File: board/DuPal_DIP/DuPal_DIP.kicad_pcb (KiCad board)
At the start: 2 copper layers, 113 x 78.7 mm, 56 parts, among them J1 AVR-ISP-6, J2 RS232, J3 Power IN, SW1 SW_Push, SW2 Power, U1 ATmega8A-PU, U10 24 Pin PAL, U2 74HC595, U3 74HC595, U5 20 Pin PAL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

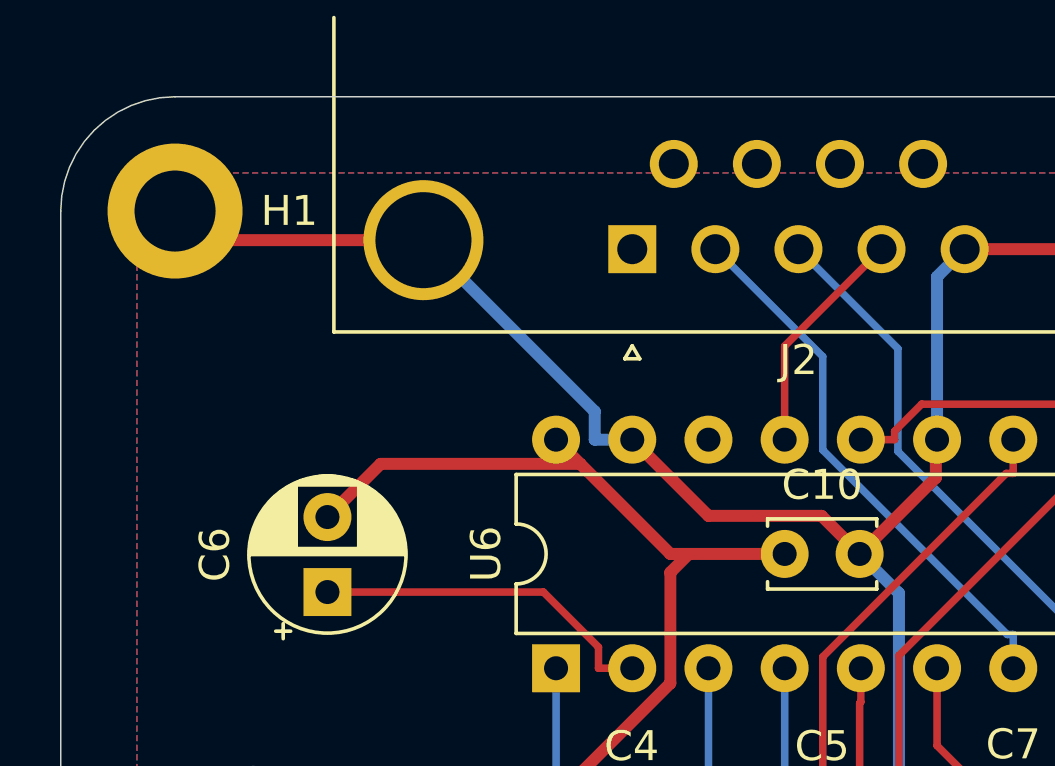
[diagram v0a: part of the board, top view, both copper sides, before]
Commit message: Updated silkscreen
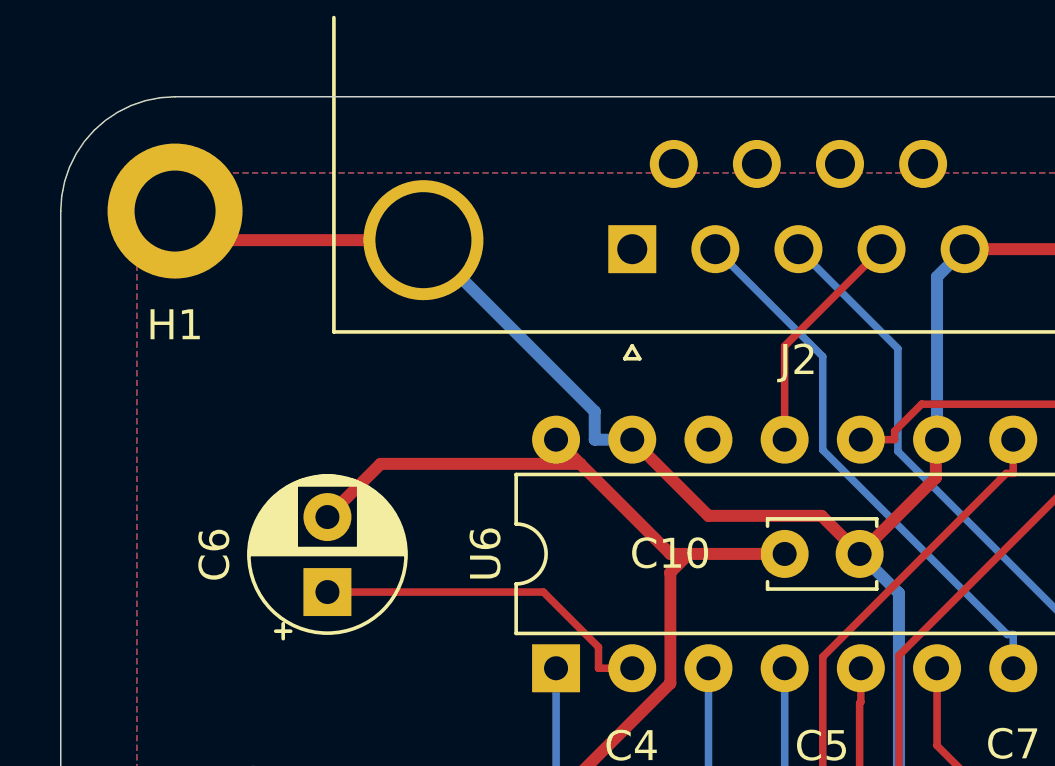
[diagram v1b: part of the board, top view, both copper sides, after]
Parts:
- added G***: LOGO, logo:logo, B.Cu at (205.7, 91.4)
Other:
- board text added: "CC-BY-SA-4.0"
